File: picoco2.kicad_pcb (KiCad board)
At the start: 2 copper layers, 54 x 102.9 mm, 40 parts, among them J1 Conn_01x03_Female, J2 Micro_SD_Card, J3 Conn_01x03_Female, Q1 Q_NMOS_GDS, SW1 SW_Push, SW2 SW_Push, U1 PicoW, U2 scd30, U3 ssd1306, U4 PCF8523T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

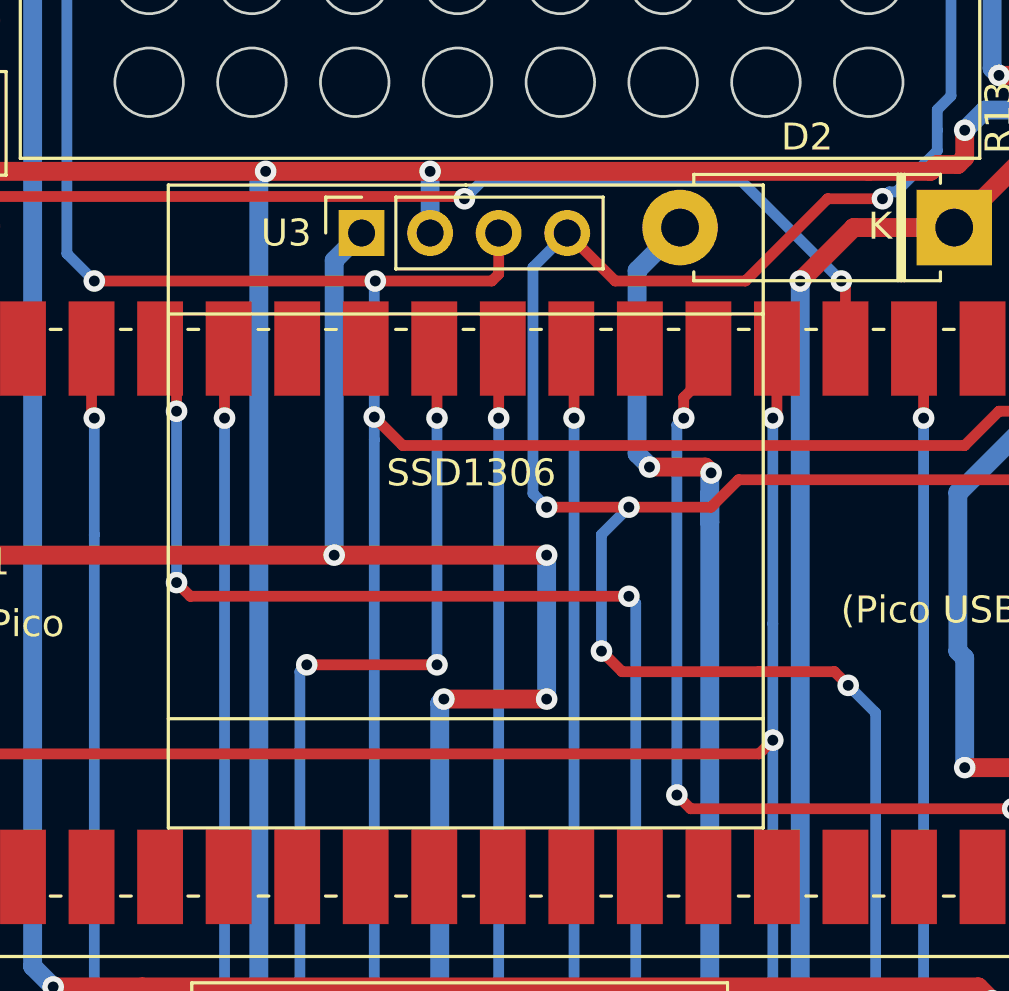
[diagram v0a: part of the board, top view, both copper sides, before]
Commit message: recentered the display
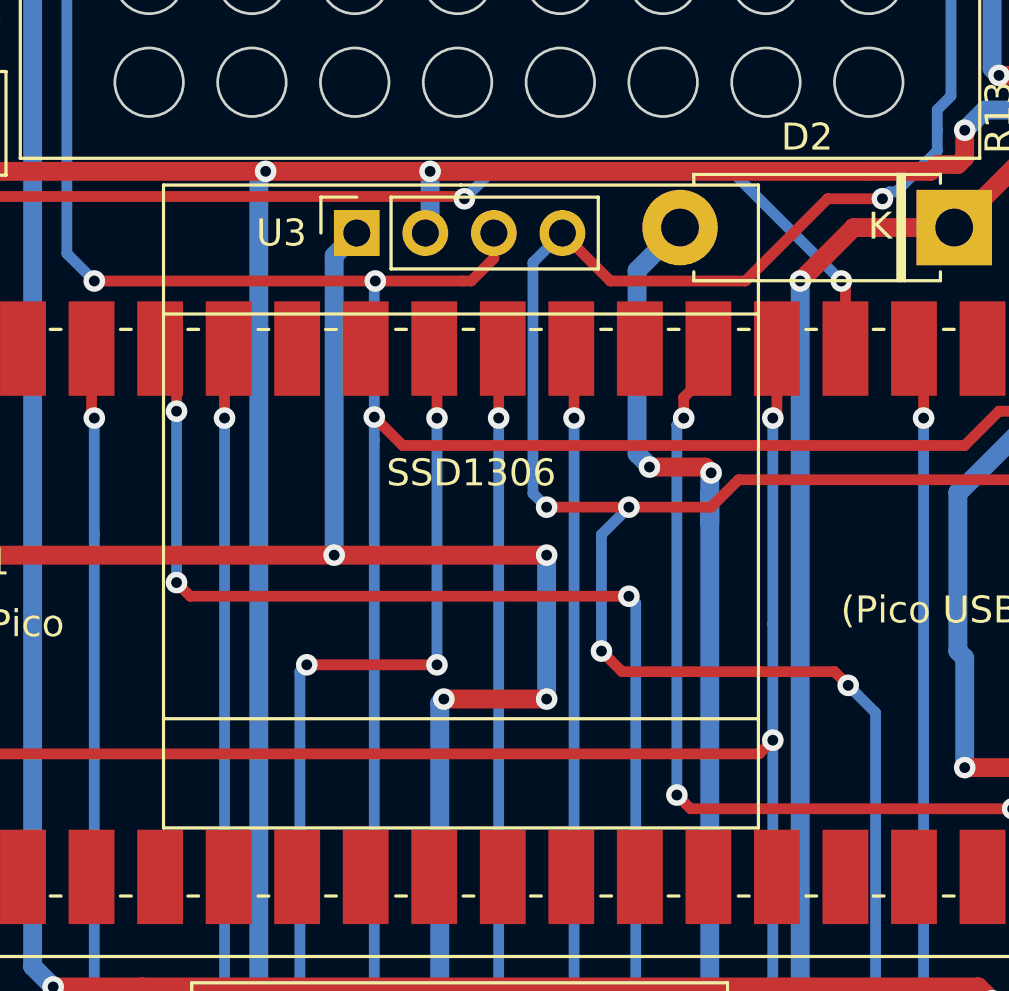
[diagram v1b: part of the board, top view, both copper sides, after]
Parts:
- moved U3 0.18 mm to (23.2, 26.9)
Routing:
- net SCL: track 164.0 -> 163.5 mm

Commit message: cover, revised base, back
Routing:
- net SDA: track 197.2 -> 196.5 mm, vias 14 -> 13
